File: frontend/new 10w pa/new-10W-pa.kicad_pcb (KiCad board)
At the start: 2 copper layers, 100 x 100 mm, 184 parts, among them CN1 BREAKOUT, K1 D3002, K2 D3002, K3 D3002, K4 D3002, K5 D3002, K6 D3002, K7 D3002, P1 CONN_01X02, P2 CONN_02X01, P4 CONN_01X02, P5 CONN_01X02, Q1 2N7000, Q3 RD16HHF1, Q4 2N7000, T1 TRANSFO, T2 OUT_TRANSF, U1 4050, U2 74LS145, U3 74LS145, U7 LP2951-50D

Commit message: BOM and PCB updates
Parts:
- moved U2 0.90 mm to (157.5, 100.5)
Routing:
- net (no net): track 77.7 -> 0.67 mm, vias 16 -> 0
- net GND: track 132.0 -> 206.6 mm, vias 47 -> 62
- net Net-(K3-Pad10): track 44.0 -> 46.1 mm
- net D: track 47.3 -> 48.6 mm
- net C: track 41.3 -> 40.1 mm
- net Net-(K7-Pad10): track 46.7 -> 45.5 mm
- net Net-(K2-Pad10): track 63.4 -> 64.4 mm
- net Net-(K6-Pad10): track 31.4 -> 30.7 mm
- net A: track 39.0 -> 39.7 mm
- net Net-(K4-Pad10): track 25.5 -> 26.1 mm

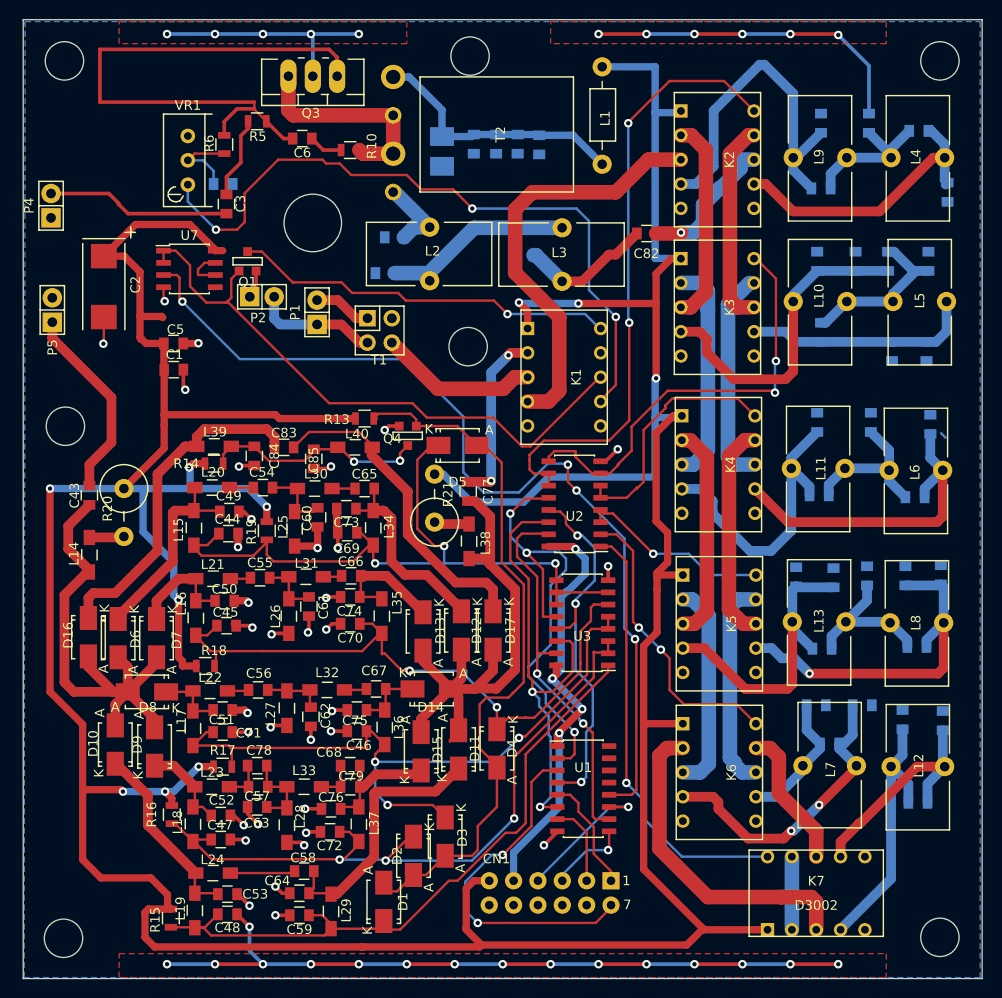
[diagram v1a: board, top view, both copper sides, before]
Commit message: Added opto and change of PTT
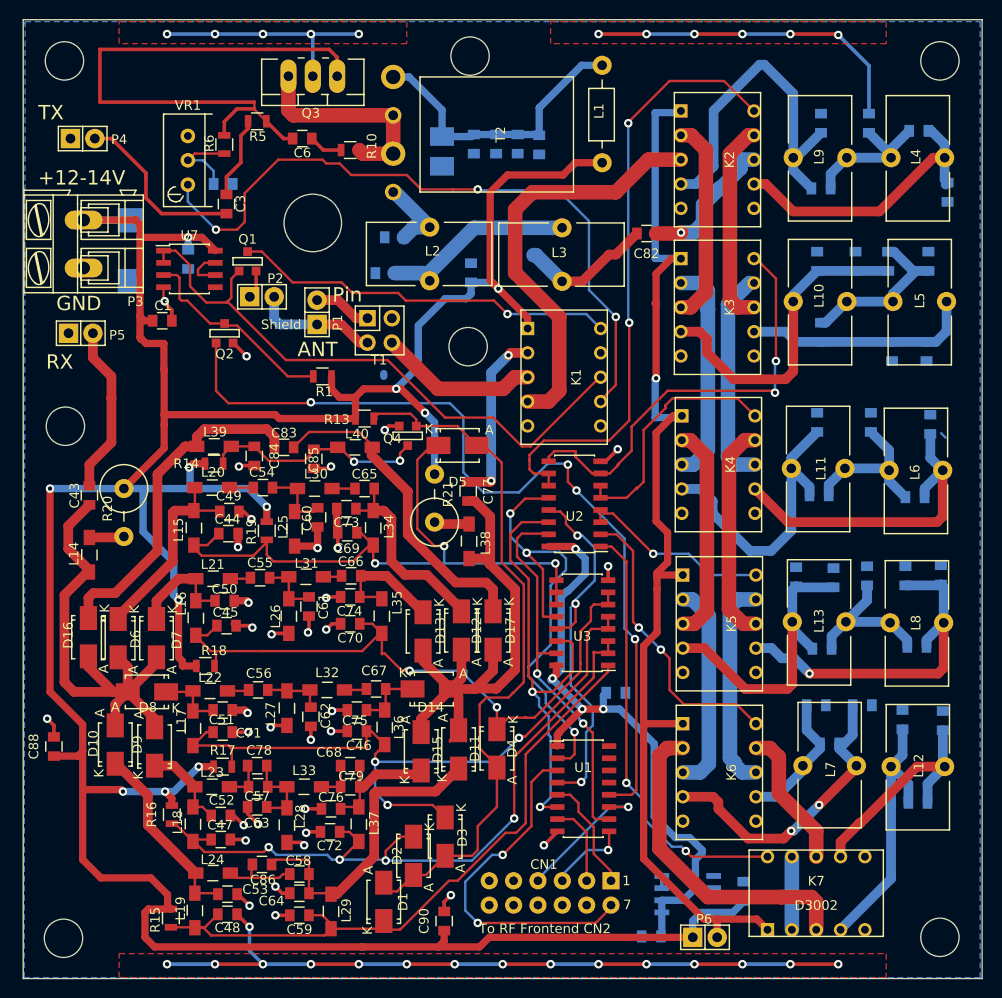
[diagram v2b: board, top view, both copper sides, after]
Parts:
- added C86: 150pF, HERMESLITE:C_0805, F.Cu at (124.9, 138.1)
- added C87: 0.1uF, HERMESLITE:C_0805, B.Cu at (175.1, 140.9)
- added C88: 0.1uF, HERMESLITE:C_0805, F.Cu at (103.2, 125.8)
- added C89: 0.1uF, HERMESLITE:C_0805, B.Cu at (146.7, 76.4)
- added C90: 0.1uF, HERMESLITE:C_0805, F.Cu at (143.9, 144.0)
- added C91: 0.1uF, HERMESLITE:C_0805, B.Cu at (165.5, 145.6)
- added C92: 0.1uF, HERMESLITE:C_0805, B.Cu at (161.8, 120.2)
- added P3: External 12V-13.8V (OSTTC022162), Connect:AK300-2, F.Cu at (106.3, 75.9)
- added P6: TX Filter Activate Jumper, Pin_Headers:Pin_Header_Straight_1x02, F.Cu at (171.1, 145.7)
- added Q2: FDV301, SMD_Packages:SOT-23-GDS, F.Cu at (121.0, 82.7)
- added R1: 10k, HERMESLITE:R_0805, F.Cu at (131.2, 87.2)
- added U6: LP2951-50D, Housings_SOIC:SOIC-8_3.9x4.9mm_Pitch1.27mm, B.Cu at (169.3, 141.2)
- C2, C5: moved to B.Cu
- C58: value 300pF -> 150pF
- L40: value 4700uH -> 4700nH
- Q1, Q4: value 2N7000 -> FDV301
- moved C5 8.90 mm to (117.2, 75.0), turned to 270 degrees
- moved P4 7.74 mm to (106.2, 62.4), turned to 0 degrees
- moved C1 5.24 mm to (114.5, 81.4)
- moved C2 4.67 mm to (111.2, 74.1)
- moved P5 3.83 mm to (106.0, 82.7), turned to 0 degrees
- moved C58 0.58 mm to (128.8, 139.1)
- turned L1 to 90 degrees
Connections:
- CN1 pad 5: 5V -> Net-(CN1-Pad5)
- CN1 pad 6: +12V -> Net-(CN1-Pad6)
- K2 pad 1: +12V -> Net-(K2-Pad1)
- K3 pad 1: +12V -> Net-(K2-Pad1)
- K4 pad 1: +12V -> Net-(K2-Pad1)
- K5 pad 1: +12V -> Net-(K2-Pad1)
- K6 pad 1: +12V -> Net-(K2-Pad1)
- K7 pad 1: +12V -> Net-(K2-Pad1)
- P5 pad 1: RX-OUT -> GND
- P5 pad 2: GND -> RX-OUT
- U1 pad 12: Net-(U1-Pad12) -> Net-(Q2-PadG)
- U3 pad 7: Net-(C44-Pad1) -> Net-(C45-Pad1)
- U7 pad 3: Net-(U1-Pad12) -> Net-(Q2-PadD)
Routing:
- net Net-(K2-Pad1): track 0.00 -> 117.4 mm, vias 0 -> 1
- net Net-(U1-Pad12): track 97.5 -> 0.00 mm, vias 4 -> 0
- net +12V: track 437.4 -> 340.2 mm, vias 10 -> 11
- net Net-(Q2-PadG): track 0.00 -> 91.0 mm, vias 0 -> 4
- net Net-(Q2-PadD): track 0.00 -> 21.3 mm
- net 5V: track 47.1 -> 66.6 mm
- net Net-(C44-Pad1): track 73.9 -> 68.5 mm
- net Net-(C58-Pad1): track 27.7 -> 32.7 mm
- net Net-(C10-Pad1): track 27.5 -> 30.9 mm
- net GND: track 206.6 -> 209.4 mm
- net RX-OUT: track 20.6 -> 17.8 mm
- net Net-(C47-Pad1): track 74.6 -> 76.3 mm, vias 3 -> 4
- net Net-(U6-Pad6): track 0.00 -> 1.27 mm
- net Net-(C45-Pad1): track 68.4 -> 69.7 mm
- net Net-(C58-Pad2): track 6.78 -> 8.01 mm
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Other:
- board text added: "+12-14V"
- board text added: "ANT"
- board text added: "GND"
- board text added: "Pin"
- board text added: "RX"
- board text added: "Shield"
- board text added: "TX"
- board text added: "To RF Frontend CN2"

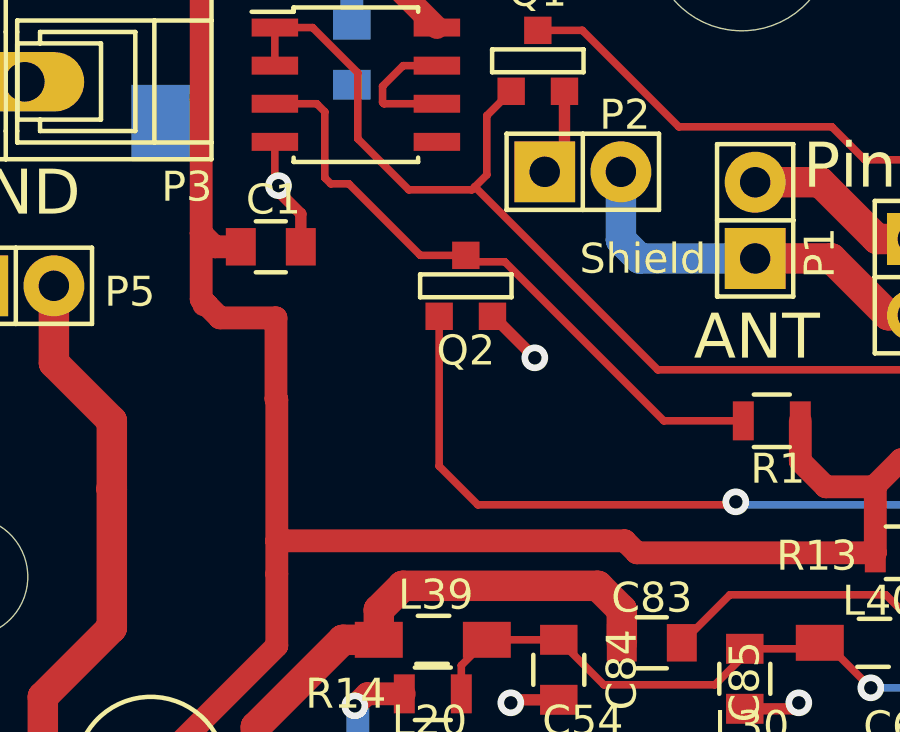
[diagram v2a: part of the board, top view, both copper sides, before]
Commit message: modify mounting holes
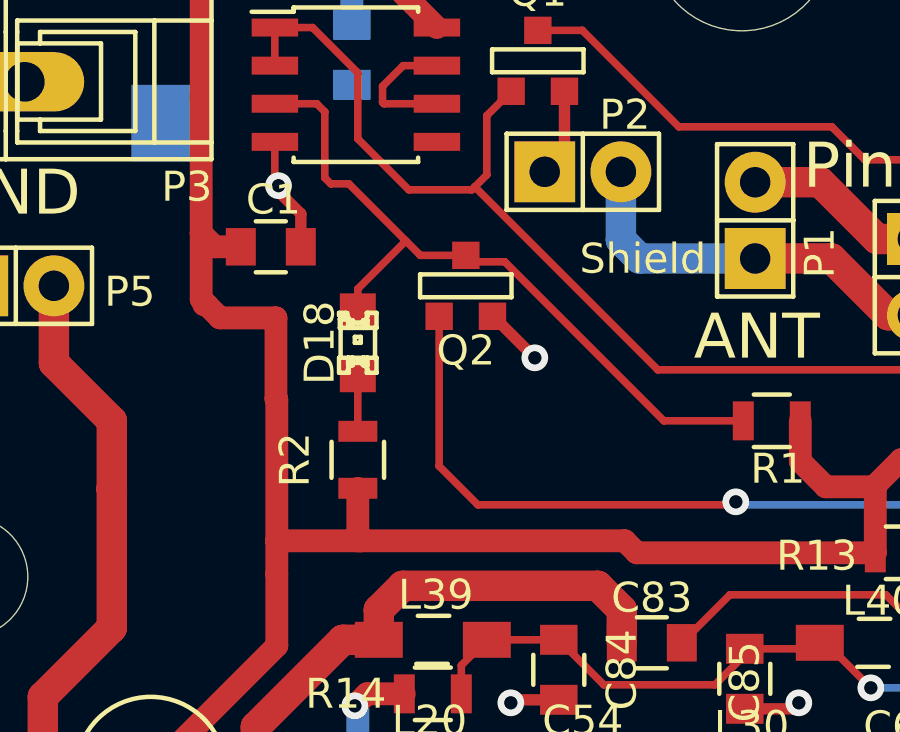
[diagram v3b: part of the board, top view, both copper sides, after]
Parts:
- added D18: RED LED (PTT), LEDs:LED-0805, F.Cu at (117.4, 84.6)
- added R2: 4.99k, HERMESLITE:R_0805, F.Cu at (117.4, 88.5)
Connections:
- net GND renamed VSS
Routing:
- net Net-(D18-Pad2): track 21.3 -> 24.3 mm
- net +12V: track 340.2 -> 342.2 mm
- net Net-(D18-Pad1): track 0.00 -> 1.90 mm
- added copper zone on F.Cu, net GND
- removed copper zone on F.Cu, net VSS
